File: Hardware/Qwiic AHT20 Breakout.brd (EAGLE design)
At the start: 25.4 x 25.4 mm, 41 parts, among them J2 QWIIC_RIGHT_ANGLE, J3 PTH, J4 QWIIC_RIGHT_ANGLE, U2 AHT20QFN-6

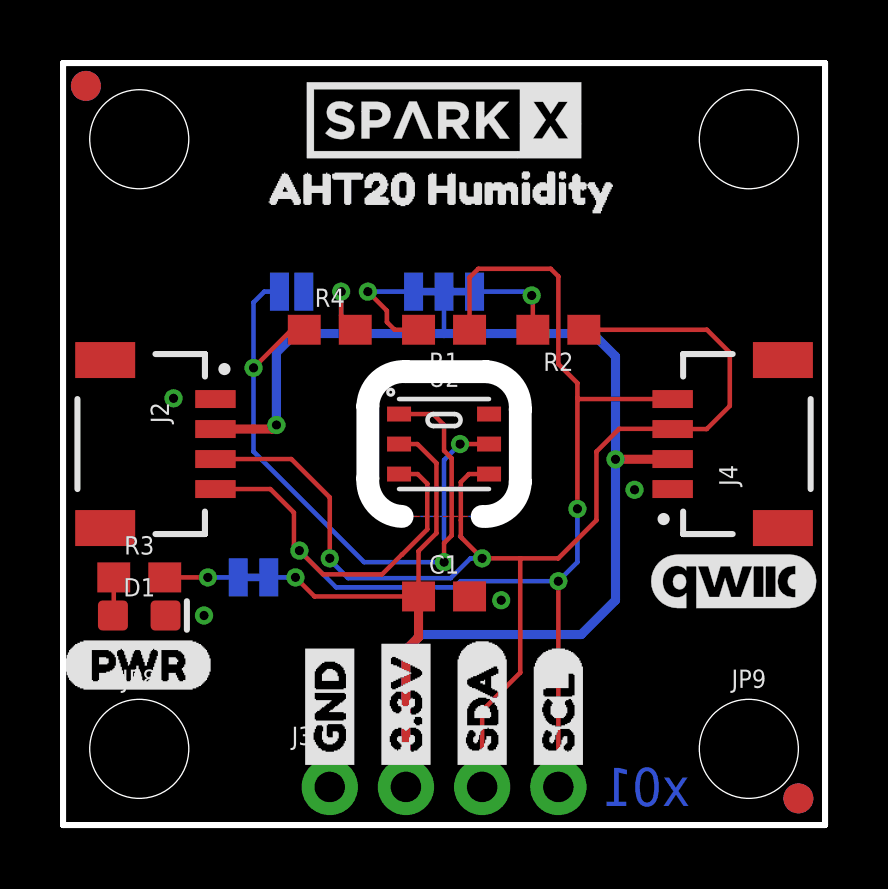
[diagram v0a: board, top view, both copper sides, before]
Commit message: Fix FP of IC to correct 2mm pad spacing
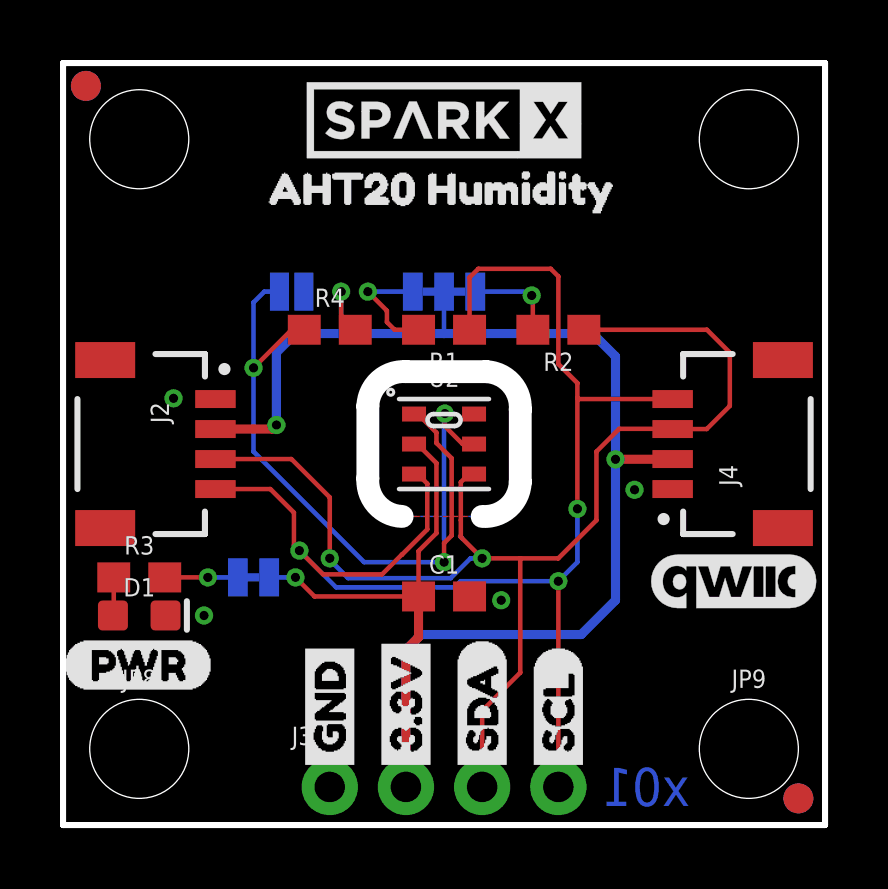
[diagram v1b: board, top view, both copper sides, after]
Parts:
- LED: value (none) -> JUMPER-SMT_2_NC_TRACE_SILK
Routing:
- net GND: track 4.51 -> 5.99 mm
- net N$5: track 22.5 -> 21.7 mm
- net 3.3V: track 60.9 -> 60.4 mm
- net SDA: track 42.7 -> 42.2 mm
- net SCL: track 47.0 -> 46.5 mm
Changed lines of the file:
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@@
 <?xml version="1.0" encoding="utf-8"?>
 <!DOCTYPE eagle SYSTEM "eagle.dtd">
-<eagle version="9.5.2">
+<eagle version="9.6.0">
 <drawing>
 <settings>
@@
 <layer number="44" name="Drills" color="7" fill="1" visible="no" active="yes"/>
 <layer number="45" name="Holes" color="7" fill="1" visible="yes" active="yes"/>
-<layer number="46" name="Milling" color="3" fill="1" visible="yes" active="yes"/>
+<layer number="46" name="Milling" color="3" fill="1" visible="no" active="yes"/>
 <layer number="47" name="Measures" color="7" fill="1" visible="no" active="yes"/>
 <layer number="48" name="Document" color="7" fill="1" visible="no" active="yes"/>
@@
 <attribute name="VALUE" x="22.86" y="0.508" size="0.6096" layer="27" font="vector" ratio="20" align="top-center"/>
 </element>
-<element name="LED" library="SparkFun-Jumpers" package="SMT-JUMPER_2_NC_TRACE_SILK" package3d_urn="urn:adsk.eagle:package:39281/1" value="" x="6.35" y="8.255" smashed="yes" rot="MR180">
+<element name="LED" library="SparkFun-Jumpers" package="SMT-JUMPER_2_NC_TRACE_SILK" package3d_urn="urn:adsk.eagle:package:39281/1" value="JUMPER-SMT_2_NC_TRACE_SILK" x="6.35" y="8.255" smashed="yes" rot="MR180">
 <attribute name="NAME" x="6.35" y="7.112" size="0.6096" layer="26" font="vector" ratio="20" rot="MR180" align="bottom-center"/>
 <attribute name="VALUE" x="6.35" y="9.398" size="0.6096" layer="28" font="vector" ratio="20" rot="MR180" align="top-center"/>
@@
 <contactref element="U2" pad="VDD"/>
 <contactref element="R4" pad="2"/>
-<wire x1="11.2" y1="12.7" x2="11.811" y2="12.7" width="0.1524" layer="1"/>
+<wire x1="11.7" y1="12.7" x2="11.811" y2="12.7" width="0.1524" layer="1"/>
 <wire x1="11.85" y1="9.13294375" x2="11.85" y2="7.62" width="0.1524" layer="1"/>
 <wire x1="5.08" y1="13.2" x2="6.977" y2="13.2" width="0.3048" layer="1"/>
@@
 <wire x1="8.382" y1="7.62" x2="7.747" y2="8.255" width="0.1524" layer="1"/>
 <via x="7.747" y="8.255" extent="1-16" drill="0.3048"/>
-<wire x1="6.858" y1="8.255" x2="7.747" y2="8.255" width="0.1524" layer="16"/>
+<wire x1="6.8707" y1="8.255" x2="7.747" y2="8.255" width="0.1524" layer="16"/>
 <wire x1="12.7" y1="17.78" x2="12.7" y2="16.383" width="0.1524" layer="16"/>
 <wire x1="9.74" y1="16.51" x2="9.271" y2="16.979" width="0.1524" layer="1"/>
@@
 <contactref element="U2" pad="GND"/>
 <contactref element="ADR" pad="1"/>
-<wire x1="14.2" y1="12.7" x2="13.2334" y2="12.7" width="0.1524" layer="1"/>
-<via x="13.2334" y="12.7" extent="1-16" drill="0.3048"/>
+<wire x1="13.7" y1="12.7" x2="13.319" y2="12.7" width="0.1524" layer="1"/>
+<wire x1="13.319" y1="12.7" x2="12.7254" y2="13.2936" width="0.1524" layer="1"/>
+<wire x1="12.7254" y1="13.2936" x2="12.7254" y2="13.716" width="0.1524" layer="1"/>
+<via x="12.7254" y="13.716" extent="1-16" drill="0.3048"/>
 <via x="14.605" y="7.493" extent="1-16" drill="0.3048"/>
 <via x="19.05" y="11.176" extent="1-16" drill="0.3048"/>
@@
 <via x="3.683" y="14.224" extent="1-16" drill="0.3048"/>
 <wire x1="13.2334" y1="9.6266" x2="13.335" y2="9.525" width="0.1524" layer="16"/>
-<wire x1="13.2334" y1="12.7" x2="12.7" y2="12.1666" width="0.1524" layer="16"/>
-<wire x1="12.7" y1="12.1666" x2="12.7" y2="9.525" width="0.1524" layer="16"/>
+<wire x1="12.7254" y1="13.716" x2="12.7" y2="13.6906" width="0.1524" layer="16"/>
+<wire x1="12.7" y1="13.6906" x2="12.7" y2="9.525" width="0.1524" layer="16"/>
 </signal>
 <signal name="SCL">
@@
 <contactref element="R1" pad="1"/>
 <contactref element="U2" pad="SCL"/>
-<wire x1="11.2" y1="11.7" x2="11.8204" y2="11.7" width="0.1524" layer="1"/>
+<wire x1="11.7" y1="11.7" x2="11.8204" y2="11.7" width="0.1524" layer="1"/>
 <wire x1="11.8204" y1="11.7" x2="12.1412" y2="11.3792" width="0.1524" layer="1"/>
 <wire x1="5.08" y1="11.2" x2="6.9102" y2="11.2" width="0.1524" layer="1"/>
@@
 <wire x1="8.89" y1="8.89" x2="8.89" y2="8.83994375" width="0.1524" layer="16"/>
 <wire x1="9.50034375" y1="8.2296" x2="12.92094375" y2="8.2296" width="0.1524" layer="16"/>
-<wire x1="14.2" y1="11.7" x2="13.5288" y2="11.7" width="0.1524" layer="1"/>
+<wire x1="13.7" y1="11.7" x2="13.5288" y2="11.7" width="0.1524" layer="1"/>
 <wire x1="13.5288" y1="11.7" x2="13.2588" y2="11.43" width="0.1524" layer="1"/>
 <wire x1="13.2588" y1="11.43" x2="13.2588" y2="10.16" width="0.1524" layer="1"/>
@@
 <contactref element="R1" pad="2"/>
 <contactref element="JP7" pad="3"/>
-<wire x1="11.684" y1="17.78" x2="10.16" y2="17.78" width="0.1524" layer="16"/>
+<wire x1="11.6586" y1="17.78" x2="10.16" y2="17.78" width="0.1524" layer="16"/>
 <via x="10.16" y="17.78" extent="1-16" drill="0.3048"/>
 <wire x1="11.85" y1="16.51" x2="11.049" y2="16.51" width="0.1524" layer="1"/>
@@
 <contactref element="R2" pad="2"/>
 <contactref element="JP7" pad="1"/>
-<wire x1="13.716" y1="17.78" x2="15.494" y2="17.78" width="0.1524" layer="16"/>
+<wire x1="13.7414" y1="17.78" x2="15.494" y2="17.78" width="0.1524" layer="16"/>
 <wire x1="15.494" y1="17.78" x2="15.621" y2="17.653" width="0.1524" layer="16"/>
 <via x="15.621" y="17.653" extent="1-16" drill="0.3048"/>
@@
 <wire x1="3.39" y1="8.255" x2="4.826" y2="8.255" width="0.1524" layer="1"/>
 <via x="4.826" y="8.255" extent="1-16" drill="0.3048"/>
-<wire x1="5.842" y1="8.255" x2="4.826" y2="8.255" width="0.1524" layer="16"/>
+<wire x1="5.8293" y1="8.255" x2="4.826" y2="8.255" width="0.1524" layer="16"/>
 </signal>
 <signal name="N$5">
@@
 <contactref element="ADR" pad="2"/>
 <contactref element="R4" pad="1"/>
-<wire x1="11.2" y1="13.7" x2="12.335" y2="13.7" width="0.1524" layer="1"/>
-<wire x1="12.335" y1="13.7" x2="12.7" y2="13.335" width="0.1524" layer="1"/>
+<wire x1="11.7" y1="13.7" x2="11.827" y2="13.7" width="0.1524" layer="1"/>
+<wire x1="11.827" y1="13.7" x2="12.446" y2="13.081" width="0.1524" layer="1"/>
 <via x="12.7" y="8.763" extent="1-16" drill="0.3048"/>
 <wire x1="8.04" y1="16.51" x2="7.62" y2="16.51" width="0.1524" layer="1"/>
@@
 <wire x1="7.2136" y1="17.78" x2="6.7056" y2="17.78" width="0.1524" layer="16"/>
 <wire x1="6.7056" y1="17.78" x2="6.35" y2="17.4244" width="0.1524" layer="16"/>
-<wire x1="12.7" y1="12.47905625" x2="12.954" y2="12.22505625" width="0.1524" layer="1"/>
-<wire x1="12.7" y1="13.335" x2="12.7" y2="12.47905625" width="0.1524" layer="1"/>
+<wire x1="12.446" y1="12.73305625" x2="12.954" y2="12.22505625" width="0.1524" layer="1"/>
+<wire x1="12.446" y1="13.081" x2="12.446" y2="12.73305625" width="0.1524" layer="1"/>
 <wire x1="12.954" y1="9.652" x2="12.7" y2="9.398" width="0.1524" layer="1"/>
 <wire x1="12.7" y1="9.398" x2="12.7" y2="8.763" width="0.1524" layer="1"/>

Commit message: Fix FP spacing. Remove experimental ADR feature. Update version number.
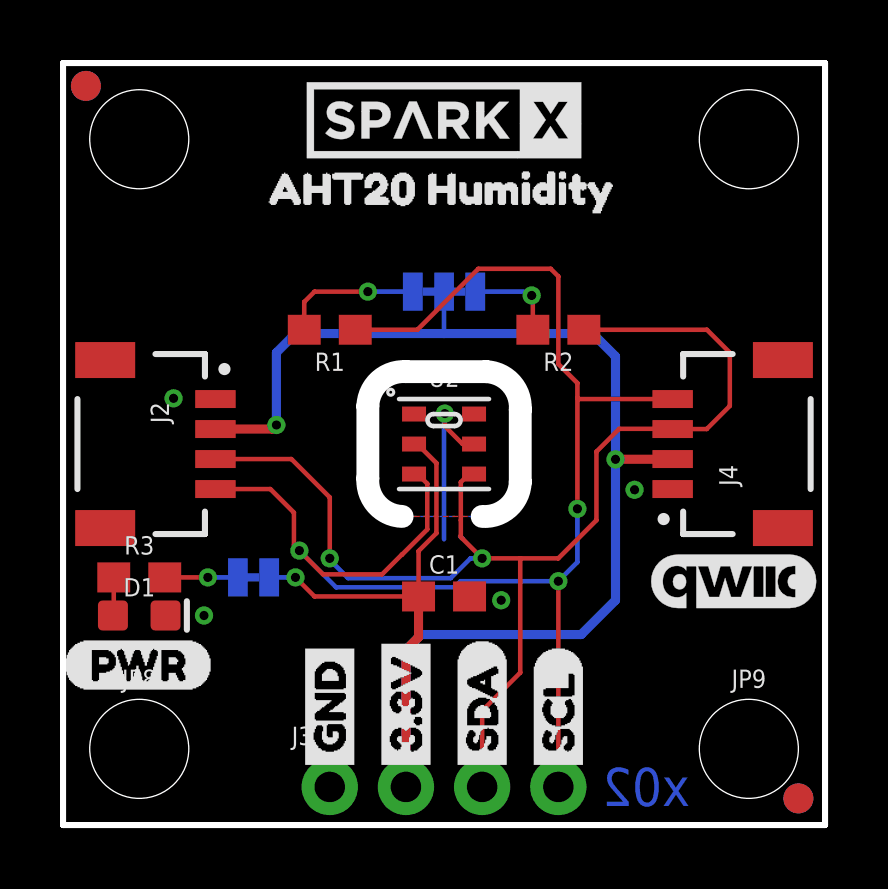
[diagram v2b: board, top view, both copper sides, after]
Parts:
- removed ADR: (no value), SparkFun-Jumpers:SMT-JUMPER_2_NO_SILK
- removed R4: 10k, SparkFun-Resistors:0603
- removed U$13: (no value), Labels:ADR-()-03
- moved R1 3.81 mm to (8.89, 16.5)
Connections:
- removed net N$5: ADR.2, R4.1, U2.ADR
- net 3.3V: no longer R4.2
- net GND: no longer ADR.1
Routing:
- net N$5: track 21.7 -> 0.00 mm, vias 2 -> 0
- net 3.3V: track 60.4 -> 57.5 mm, vias 4 -> 3
- net SCL: track 46.5 -> 49.3 mm
- net N$1: track 3.94 -> 4.69 mm
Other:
- board text added: "x02"
- board text removed: "x01"
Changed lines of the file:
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@@
 <wire x1="25.4" y1="25.4" x2="25.4" y2="0" width="0.2032" layer="20"/>
 <wire x1="25.4" y1="0" x2="0" y2="0" width="0.2032" layer="20"/>
-<text x="19.431" y="1.27" size="1.27" layer="16" font="vector" ratio="15" rot="MR0" align="center">x01</text>
+<text x="19.431" y="1.27" size="1.27" layer="16" font="vector" ratio="15" rot="MR0" align="center">x02</text>
 <dimension x1="0" y1="0" x2="0" y2="25.4" x3="-5.08" y3="12.7" textsize="1.778" textratio="15" layer="47" unit="inch"/>
 <dimension x1="2.54" y1="22.86" x2="2.54" y2="0" x3="-1.27" y3="11.43" textsize="1.778" textratio="15" layer="47" unit="inch"/>
@@
 </element>
 <element name="U$10" library="Labels-0_04" package="(PWR)" value="" x="0" y="5.334" smashed="yes"/>
-<element name="R1" library="SparkFun-Resistors" package="0603" value="2.2k" x="12.7" y="16.51" smashed="yes" rot="R180">
-<attribute name="NAME" x="12.7" y="15.748" size="0.6096" layer="25" font="vector" ratio="20" rot="R180" align="bottom-center"/>
-<attribute name="PROD_ID" value="RES-08272" x="12.7" y="16.51" size="1.778" layer="27" rot="R180" display="off"/>
-<attribute name="VALUE" x="12.7" y="17.272" size="0.6096" layer="27" font="vector" ratio="20" rot="R180" align="top-center"/>
+<element name="R1" library="SparkFun-Resistors" package="0603" value="2.2k" x="8.89" y="16.51" smashed="yes" rot="R180">
+<attribute name="NAME" x="8.89" y="15.748" size="0.6096" layer="25" font="vector" ratio="20" rot="R180" align="bottom-center"/>
+<attribute name="PROD_ID" value="RES-08272" x="8.89" y="16.51" size="1.778" layer="27" rot="R180" display="off"/>
+<attribute name="VALUE" x="8.89" y="17.272" size="0.6096" layer="27" font="vector" ratio="20" rot="R180" align="top-center"/>
 </element>
 <element name="R2" library="SparkFun-Resistors" package="0603" value="2.2k" x="16.51" y="16.51" smashed="yes" rot="R180">
@@
 <attribute name="VALUE" x="6.35" y="9.398" size="0.6096" layer="28" font="vector" ratio="20" rot="MR180" align="top-center"/>
 </element>
-<element name="R4" library="SparkFun-Resistors" package="0603" value="10k" x="8.89" y="16.51" smashed="yes">
-<attribute name="NAME" x="8.89" y="17.272" size="0.6096" layer="25" font="vector" ratio="20" align="bottom-center"/>
-<attribute name="PROD_ID" value="RES-00824" x="8.89" y="16.51" size="1.778" layer="27" font="vector" ratio="15" display="off"/>
-<attribute name="VALUE" x="8.89" y="15.748" size="0.6096" layer="27" font="vector" ratio="20" align="top-center"/>
-</element>
-<element name="ADR" library="SparkFun-Jumpers" package="SMT-JUMPER_2_NO_SILK" package3d_urn="urn:adsk.eagle:package:39279/1" value="" x="7.62" y="17.78" smashed="yes" rot="MR0">
-<attribute name="NAME" x="7.62" y="18.923" size="0.6096" layer="26" font="vector" ratio="20" rot="MR0" align="bottom-center"/>
-<attribute name="VALUE" x="7.62" y="16.637" size="0.6096" layer="28" font="vector" ratio="20" rot="MR0" align="top-center"/>
-</element>
 <element name="U2" library="AHT20" package="QFN-6" value="AHT20QFN-6" x="12.7" y="12.7" smashed="yes">
 <attribute name="NAME" x="12.7" y="14.605" size="0.6096" layer="25" font="vector" ratio="20" align="bottom-center"/>
@@
 <attribute name="VALUE" x="12.7" y="11.049" size="0.6096" layer="27" font="vector" ratio="20" align="top-center"/>
 </element>
-<element name="U$13" library="Labels" package="ADR-()-03" value="" x="9.398" y="19.685" smashed="yes" rot="MR0"/>
 <element name="U$14" library="buzzard_labels (17)" package="AHT20_HUMIDITY2" value="" x="5.969" y="21.209" smashed="yes"/>
 <element name="U$12" library="SparkFun-Buzzard" package="LED_32" value="" x="8.128" y="6.223" smashed="yes" rot="MR0"/>
@@
 <contactref element="LED" pad="2"/>
 <contactref element="U2" pad="VDD"/>
-<contactref element="R4" pad="2"/>
 <wire x1="11.7" y1="12.7" x2="11.811" y2="12.7" width="0.1524" layer="1"/>
 <wire x1="11.85" y1="9.13294375" x2="11.85" y2="7.62" width="0.1524" layer="1"/>
@@
 <wire x1="7.112" y1="13.335" x2="7.112" y2="15.748" width="0.3048" layer="16"/>
 <wire x1="7.112" y1="15.748" x2="7.747" y2="16.383" width="0.3048" layer="16"/>
-<wire x1="7.747" y1="16.383" x2="9.271" y2="16.383" width="0.3048" layer="16"/>
-<wire x1="9.271" y1="16.383" x2="12.7" y2="16.383" width="0.3048" layer="16"/>
+<wire x1="7.747" y1="16.383" x2="12.7" y2="16.383" width="0.3048" layer="16"/>
 <wire x1="12.7" y1="16.383" x2="17.653" y2="16.383" width="0.3048" layer="16"/>
 <wire x1="17.653" y1="16.383" x2="18.415" y2="15.621" width="0.3048" layer="16"/>
@@
 <wire x1="6.8707" y1="8.255" x2="7.747" y2="8.255" width="0.1524" layer="16"/>
 <wire x1="12.7" y1="17.78" x2="12.7" y2="16.383" width="0.1524" layer="16"/>
-<wire x1="9.74" y1="16.51" x2="9.271" y2="16.979" width="0.1524" layer="1"/>
-<wire x1="9.271" y1="16.979" x2="9.271" y2="17.78" width="0.1524" layer="1"/>
-<via x="9.271" y="17.78" extent="1-16" drill="0.3048"/>
-<wire x1="9.271" y1="17.78" x2="9.271" y2="16.383" width="0.1524" layer="16"/>
 <wire x1="11.811" y1="12.7" x2="12.446" y2="12.065" width="0.1524" layer="1"/>
 <wire x1="12.446" y1="12.065" x2="12.446" y2="9.72894375" width="0.1524" layer="1"/>
@@
 <contactref element="J4" pad="1"/>
 <contactref element="U2" pad="GND"/>
-<contactref element="ADR" pad="1"/>
 <wire x1="13.7" y1="12.7" x2="13.319" y2="12.7" width="0.1524" layer="1"/>
 <wire x1="13.319" y1="12.7" x2="12.7254" y2="13.2936" width="0.1524" layer="1"/>
@@
 <wire x1="12.1412" y1="9.8552" x2="11.303" y2="9.017" width="0.1524" layer="1"/>
 <wire x1="12.1412" y1="11.3792" x2="12.1412" y2="9.8552" width="0.1524" layer="1"/>
-<wire x1="13.55" y1="16.51" x2="13.55" y2="18.249" width="0.1524" layer="1"/>
-<wire x1="13.55" y1="18.249" x2="13.843" y2="18.542" width="0.1524" layer="1"/>
+<wire x1="9.74" y1="16.51" x2="11.811" y2="16.51" width="0.1524" layer="1"/>
+<wire x1="11.811" y1="16.51" x2="13.843" y2="18.542" width="0.1524" layer="1"/>
 <wire x1="13.843" y1="18.542" x2="16.256" y2="18.542" width="0.1524" layer="1"/>
 <wire x1="16.256" y1="18.542" x2="16.51" y2="18.288" width="0.1524" layer="1"/>
@@
 <wire x1="11.6586" y1="17.78" x2="10.16" y2="17.78" width="0.1524" layer="16"/>
 <via x="10.16" y="17.78" extent="1-16" drill="0.3048"/>
-<wire x1="11.85" y1="16.51" x2="11.049" y2="16.51" width="0.1524" layer="1"/>
-<wire x1="11.049" y1="16.51" x2="10.795" y2="16.764" width="0.1524" layer="1"/>
-<wire x1="10.795" y1="16.764" x2="10.795" y2="17.145" width="0.1524" layer="1"/>
-<wire x1="10.795" y1="17.145" x2="10.16" y2="17.78" width="0.1524" layer="1"/>
+<wire x1="8.04" y1="16.51" x2="8.04" y2="17.438" width="0.1524" layer="1"/>
+<wire x1="8.04" y1="17.438" x2="8.382" y2="17.78" width="0.1524" layer="1"/>
+<wire x1="8.382" y1="17.78" x2="10.16" y2="17.78" width="0.1524" layer="1"/>
 </signal>
 <signal name="N$2">
@@
 <wire x1="5.8293" y1="8.255" x2="4.826" y2="8.255" width="0.1524" layer="16"/>
 </signal>
-<signal name="N$5">
-<contactref element="U2" pad="ADR"/>
-<contactref element="ADR" pad="2"/>
-<contactref element="R4" pad="1"/>
-<wire x1="11.7" y1="13.7" x2="11.827" y2="13.7" width="0.1524" layer="1"/>
-<wire x1="11.827" y1="13.7" x2="12.446" y2="13.081" width="0.1524" layer="1"/>
-<via x="12.7" y="8.763" extent="1-16" drill="0.3048"/>
-<wire x1="8.04" y1="16.51" x2="7.62" y2="16.51" width="0.1524" layer="1"/>
-<wire x1="7.62" y1="16.51" x2="6.35" y2="15.24" width="0.1524" layer="1"/>
-<via x="6.35" y="15.24" extent="1-16" drill="0.3048"/>
-<wire x1="6.35" y1="15.24" x2="6.35" y2="12.446" width="0.1524" layer="16"/>
-<wire x1="10.033" y1="8.763" x2="12.7" y2="8.763" width="0.1524" layer="16"/>
-<wire x1="6.35" y1="12.446" x2="10.033" y2="8.763" width="0.1524" layer="16"/>
-<wire x1="6.35" y1="17.4244" x2="6.35" y2="15.24" width="0.1524" layer="16"/>
-<wire x1="7.2136" y1="17.78" x2="6.7056" y2="17.78" width="0.1524" layer="16"/>
-<wire x1="6.7056" y1="17.78" x2="6.35" y2="17.4244" width="0.1524" layer="16"/>
-<wire x1="12.446" y1="12.73305625" x2="12.954" y2="12.22505625" width="0.1524" layer="1"/>
-<wire x1="12.446" y1="13.081" x2="12.446" y2="12.73305625" width="0.1524" layer="1"/>
-<wire x1="12.954" y1="9.652" x2="12.7" y2="9.398" width="0.1524" layer="1"/>
-<wire x1="12.7" y1="9.398" x2="12.7" y2="8.763" width="0.1524" layer="1"/>
-<wire x1="12.954" y1="12.22505625" x2="12.954" y2="9.652" width="0.1524" layer="1"/>
-</signal>
 <signal name="N$6">

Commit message: Add x02 panel.
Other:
- board text added: "0.8mm Thickness"
- board text removed: "0.8mm board"
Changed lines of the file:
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@@
 <?xml version="1.0" encoding="utf-8"?>
 <!DOCTYPE eagle SYSTEM "eagle.dtd">
-<eagle version="9.6.0">
+<eagle version="9.6.2">
 <drawing>
 <settings>
@@
 <wire x1="15.24" y1="11.43" x2="15.24" y2="13.843" width="0.762" layer="20"/>
 <wire x1="14.097" y1="15.113" x2="11.43" y2="15.113" width="0.762" layer="20"/>
-<text x="41.91" y="38.1" size="1.778" layer="51" font="vector" ratio="15">0.8mm board</text>
+<text x="41.91" y="38.1" size="1.778" layer="51" font="vector" ratio="15">0.8mm Thickness</text>
 <wire x1="10.16" y1="11.557" x2="10.16" y2="13.97" width="0.762" layer="20"/>
 <wire x1="10.16" y1="13.97" x2="11.43" y2="15.113" width="0.762" layer="20" curve="-92.115627"/>
